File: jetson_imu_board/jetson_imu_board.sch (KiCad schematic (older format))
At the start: 9 parts

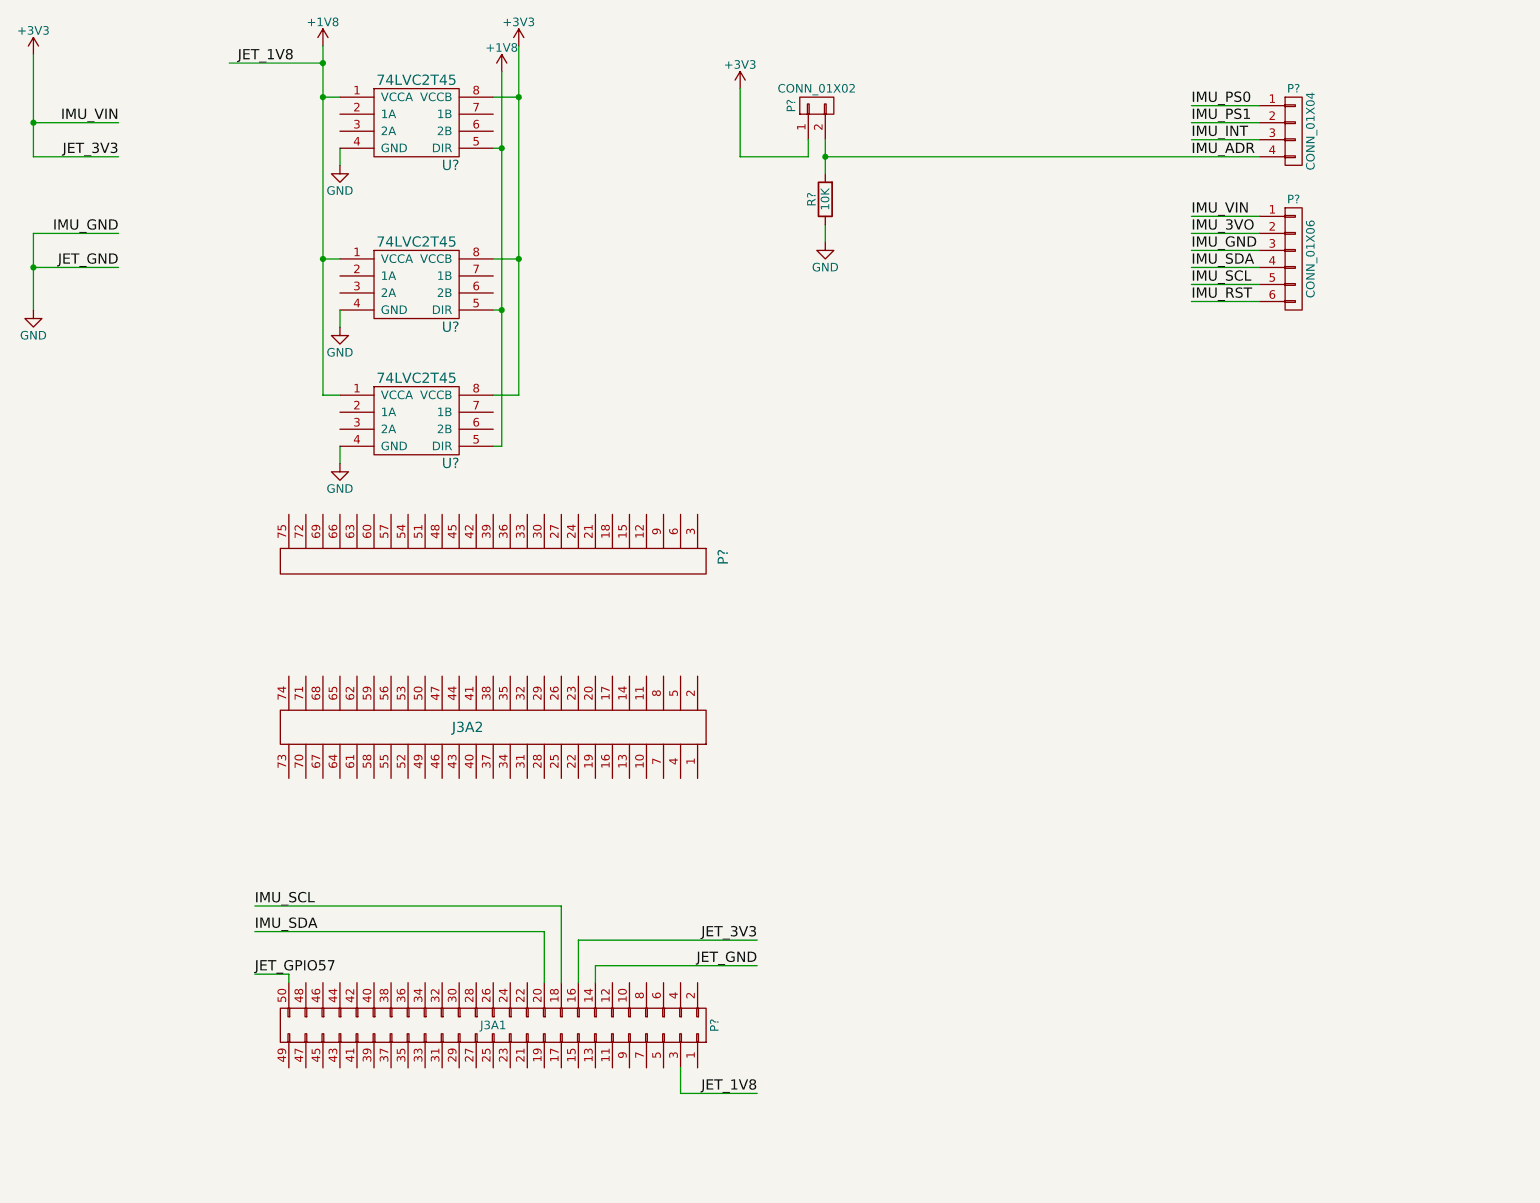
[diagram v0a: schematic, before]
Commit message: Switched to TXB0108 level shifter
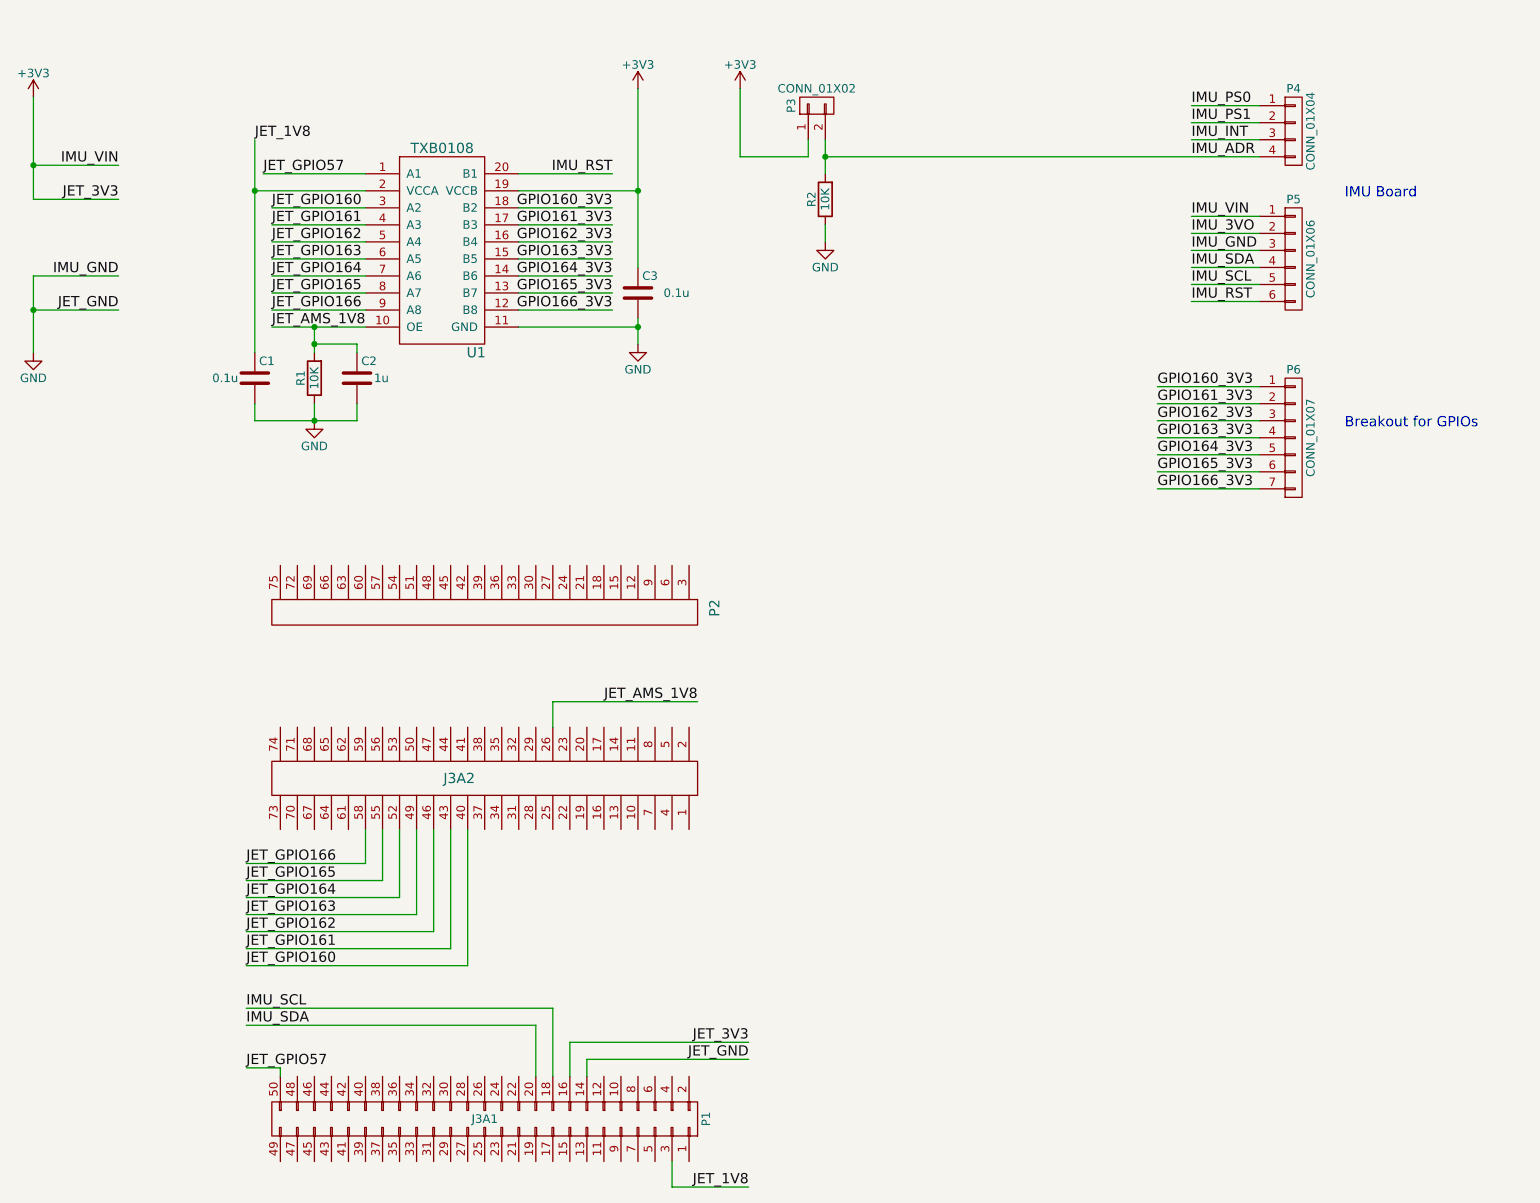
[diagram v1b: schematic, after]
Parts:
- removed U? (x3): 74LVC2T45, symbol 74LVC2T45
- added C1, C3: 0.1u, symbol C
- added C2: 1u, symbol C
- added P6: CONN_01X07, symbol CONN_01X07
- added R1: 10K, symbol R
- added U1: TXB0108, symbol TXB0108
- gave numbers to parts that had none: 6
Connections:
- net +3V3: now also C3.1, U1.19 (VCCB)
- net GND: now also C1.2, C2.2, C3.2, R1.1, U1.11 (GND)
- net IMU_RST: now also U1.20 (B1)
- net JET_GPIO57: now also U1.1 (A1)
- net JET_AMS_1V8: now reaches P2.26
- net JET_AMS_1V8: now also C2.1, R1.2, U1.10 (OE)
- net JET_GPIO160: now reaches P2.40
- net JET_GPIO160: now also U1.3 (A2)
- net JET_GPIO161: now reaches P2.43
- net JET_GPIO161: now also U1.4 (A3)
- net JET_GPIO162: now reaches P2.46
- net JET_GPIO162: now also U1.5 (A4)
- net JET_GPIO163: now reaches P2.49
- net JET_GPIO163: now also U1.6 (A5)
- net JET_GPIO164: now reaches P2.52
- net JET_GPIO164: now also U1.7 (A6)
- net JET_GPIO165: now reaches P2.55
- net JET_GPIO165: now also U1.8 (A7)
- net JET_GPIO166: now reaches P2.58
- net JET_GPIO166: now also U1.9 (A8)
- net +1V8 renamed JET_1V8
- net JET_1V8: now also C1.1, U1.2 (VCCA)
- new net GPIO160_3V3: P6.1 (P1), U1.18 (B2)
- new net GPIO161_3V3: P6.2 (P2), U1.17 (B3)
- new net GPIO162_3V3: P6.3 (P3), U1.16 (B4)
- new net GPIO163_3V3: P6.4 (P4), U1.15 (B5)
- new net GPIO164_3V3: P6.5 (P5), U1.14 (B6)
- new net GPIO165_3V3: P6.6 (P6), U1.13 (B7)
- new net GPIO166_3V3: P6.7 (P7), U1.12 (B8)
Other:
- note added: "Breakout for GPIOs"
- note added: "IMU Board"
- moved on the sheet: P1, P2

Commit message: Added footprint associations, started board layout
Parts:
- C1, C2, C3: footprint (none) -> Capacitors_SMD:C_1206_HandSoldering
- P1, P2: footprint (none) -> Pin_Headers:Pin_Header_Straight_2x25_Pitch2.00mm
- P3: footprint (none) -> Pin_Headers:Pin_Header_Straight_1x02
- P4: footprint (none) -> Pin_Headers:Pin_Header_Straight_1x04
- P5: footprint (none) -> Pin_Headers:Pin_Header_Straight_1x06
- P6: footprint (none) -> Pin_Headers:Pin_Header_Straight_1x07
- R1, R2: footprint (none) -> Resistors_SMD:R_1206_HandSoldering
- U1: footprint (none) -> Housings_SSOP:SSOP-20_4.4x6.5mm_Pitch0.65mm
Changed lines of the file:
@@
 F 0 "P1" H 3650 8350 50  0000 C CNN
 F 1 "J3A1" V 3650 7050 50  0000 C CNN
-F 2 "" H 3650 6300 50  0000 C CNN
+F 2 "Pin_Headers:Pin_Header_Straight_2x25_Pitch2.00mm" H 3650 6300 50  0001 C CNN
 F 3 "" H 3650 6300 50  0000 C CNN
 	1    3650 7050
@@
 F 0 "P2" H 4350 5600 60  0000 C CNN
 F 1 "J3A2" V 3350 4100 60  0000 C CNN
-F 2 "" H 4100 1950 60  0001 C CNN
+F 2 "Pin_Headers:Pin_Header_Straight_2x25_Pitch2.00mm" H 4100 1950 60  0001 C CNN
 F 3 "" H 4100 1950 60  0001 C CNN
 	1    3900 4500
@@
 F 0 "P4" H 8400 1500 50  0000 C CNN
 F 1 "CONN_01X04" V 8500 1250 50  0000 C CNN
-F 2 "" H 8400 1250 50  0000 C CNN
+F 2 "Pin_Headers:Pin_Header_Straight_1x04" H 8400 1250 50  0001 C CNN
 F 3 "" H 8400 1250 50  0000 C CNN
 	1    8400 1250
@@
 F 0 "P5" H 8400 2350 50  0000 C CNN
 F 1 "CONN_01X06" V 8500 2000 50  0000 C CNN
-F 2 "" H 8400 2000 50  0000 C CNN
+F 2 "Pin_Headers:Pin_Header_Straight_1x06" H 8400 2000 50  0001 C CNN
 F 3 "" H 8400 2000 50  0000 C CNN
 	1    8400 2000
@@
 IMU_RST
 $Comp
-L GND #PWR2
+L GND #PWR01
 U 1 1 580D6C71
 P 1000 2550
-F 0 "#PWR2" H 1000 2300 50  0001 C CNN
+F 0 "#PWR01" H 1000 2300 50  0001 C CNN
 F 1 "GND" H 1000 2400 50  0000 C CNN
 F 2 "" H 1000 2550 50  0000 C CNN
@@
 IMU_SDA
 $Comp
-L +3V3 #PWR1
+L +3V3 #PWR02
 U 1 1 580D6F0B
 P 1000 1050
-F 0 "#PWR1" H 1000 900 50  0001 C CNN
+F 0 "#PWR02" H 1000 900 50  0001 C CNN
 F 1 "+3V3" H 1000 1190 50  0000 C CNN
 F 2 "" H 1000 1050 50  0000 C CNN
@@
 F 0 "P3" H 5600 1250 50  0000 C CNN
 F 1 "CONN_01X02" V 5700 1100 50  0000 C CNN
-F 2 "" H 5600 1100 50  0000 C CNN
+F 2 "Pin_Headers:Pin_Header_Straight_1x02" H 5600 1100 50  0001 C CNN
 F 3 "" H 5600 1100 50  0000 C CNN
 	1    5600 1100
@@
 F 0 "R2" V 5730 1650 50  0000 C CNN
 F 1 "10K" V 5650 1650 50  0000 C CNN
-F 2 "" V 5580 1650 50  0000 C CNN
+F 2 "Resistors_SMD:R_1206_HandSoldering" V 5580 1650 50  0001 C CNN
 F 3 "" H 5650 1650 50  0000 C CNN
 	1    5650 1650
@@
 $EndComp
 $Comp
-L GND #PWR7
+L GND #PWR03
 U 1 1 580D740A
 P 5650 1900
-F 0 "#PWR7" H 5650 1650 50  0001 C CNN
+F 0 "#PWR03" H 5650 1650 50  0001 C CNN
 F 1 "GND" H 5650 1750 50  0000 C CNN
 F 2 "" H 5650 1900 50  0000 C CNN
@@
 $EndComp
 $Comp
-L +3V3 #PWR6
+L +3V3 #PWR04
 U 1 1 580D7475
 P 5150 1000
-F 0 "#PWR6" H 5150 850 50  0001 C CNN
+F 0 "#PWR04" H 5150 850 50  0001 C CNN
 F 1 "+3V3" H 5150 1140 50  0000 C CNN
 F 2 "" H 5150 1000 50  0000 C CNN
@@
 	8200 2250 7800 2250
 Wire Wire Line
-	1000 2100 1000 2300
-Wire Wire Line
-	1000 2300 1000 2550
+	1000 2100 1000 2550
 Wire Wire Line
 	1000 2100 1500 2100
@@
 	3950 6500 2250 6500
 Wire Wire Line
-	1000 1050 1000 1450
-Wire Wire Line
-	1000 1450 1000 1650
+	1000 1050 1000 1650
 Wire Wire Line
 	1000 1650 1500 1650
@@
 Connection ~ 1000 1450
 Wire Wire Line
-	5650 1300 5650 1400
-Wire Wire Line
-	5650 1400 5650 1500
+	5650 1300 5650 1500
 Wire Wire Line
 	5650 1400 8200 1400
@@
 F 0 "U1" H 3600 1450 60  0000 C CNN
 F 1 "TXB0108" H 3400 2650 60  0000 C CNN
-F 2 "" H 3400 1100 60  0001 C CNN
+F 2 "Housings_SSOP:SSOP-20_4.4x6.5mm_Pitch0.65mm" H 3400 1100 60  0001 C CNN
 F 3 "" H 3400 1100 60  0001 C CNN
 	1    3400 2000
@@
 	3850 1600 4550 1600
 Wire Wire Line
-	4550 1000 4550 1600
-Wire Wire Line
-	4550 1600 4550 2050
-$Comp
-L +3V3 #PWR4
+	4550 1000 4550 2050
+$Comp
+L +3V3 #PWR05
 U 1 1 580EBAD8
 P 4550 1000
-F 0 "#PWR4" H 4550 850 50  0001 C CNN
+F 0 "#PWR05" H 4550 850 50  0001 C CNN
 F 1 "+3V3" H 4550 1140 50  0000 C CNN
 F 2 "" H 4550 1000 50  0000 C CNN
@@
 F 0 "C3" H 4575 2300 50  0000 L CNN
 F 1 "0.1u" H 4700 2200 50  0000 L CNN
-F 2 "" H 4588 2050 50  0000 C CNN
+F 2 "Capacitors_SMD:C_1206_HandSoldering" H 4588 2050 50  0001 C CNN
 F 3 "" H 4550 2200 50  0000 C CNN
 	1    4550 2200
@@
 $EndComp
 $Comp
-L GND #PWR5
+L GND #PWR06
 U 1 1 580EBB51
 P 4550 2500
-F 0 "#PWR5" H 4550 2250 50  0001 C CNN
+F 0 "#PWR06" H 4550 2250 50  0001 C CNN
 F 1 "GND" H 4550 2350 50  0000 C CNN
 F 2 "" H 4550 2500 50  0000 C CNN
@@
 $EndComp
 Wire Wire Line
-	2300 1300 2300 1600
-Wire Wire Line
-	2300 1600 2300 2550
+	2300 1300 2300 2550
 Connection ~ 2300 1600
 Wire Wire Line
-	4550 2350 4550 2400
-Wire Wire Line
-	4550 2400 4550 2500
+	4550 2350 4550 2500
 Wire Wire Line
 	2350 1500 2950 1500
@@
 F 0 "C1" H 2325 2800 50  0000 L CNN
 F 1 "0.1u" H 2050 2700 50  0000 L CNN
-F 2 "" H 2338 2550 50  0000 C CNN
+F 2 "Capacitors_SMD:C_1206_HandSoldering" H 2338 2550 50  0001 C CNN
 F 3 "" H 2300 2700 50  0000 C CNN
 	1    2300 2700
@@
 F 0 "R1" V 2730 2700 50  0000 C CNN
 F 1 "10K" V 2650 2700 50  0000 C CNN
-F 2 "" V 2580 2700 50  0000 C CNN
+F 2 "Resistors_SMD:R_1206_HandSoldering" V 2580 2700 50  0001 C CNN
 F 3 "" H 2650 2700 50  0000 C CNN
 	1    2650 2700
@@
 $EndComp
 Wire Wire Line
-	2650 2400 2650 2500
-Wire Wire Line
-	2650 2500 2650 2550
-$Comp
-L GND #PWR3
+	2650 2400 2650 2550
+$Comp
+L GND #PWR07
 U 1 1 580EC104
 P 2650 2950
-F 0 "#PWR3" H 2650 2700 50  0001 C CNN
+F 0 "#PWR07" H 2650 2700 50  0001 C CNN
 F 1 "GND" H 2650 2800 50  0000 C CNN
 F 2 "" H 2650 2950 50  0000 C CNN
@@
 	2300 2850 2300 2950
 Wire Wire Line
-	2300 2950 2650 2950
-Wire Wire Line
-	2650 2950 2900 2950
+	2300 2950 2900 2950
 Wire Wire Line
 	2650 2850 2650 2950
 Wire Wire Line
-	2400 2400 2650 2400
-Wire Wire Line
-	2650 2400 2950 2400
+	2400 2400 2950 2400
 Connection ~ 2650 2400
 Wire Wire Line
@@
 F 0 "C2" H 2925 2800 50  0000 L CNN
 F 1 "1u" H 3000 2700 50  0000 L CNN
-F 2 "" H 2938 2550 50  0000 C CNN
+F 2 "Capacitors_SMD:C_1206_HandSoldering" H 2938 2550 50  0001 C CNN
 F 3 "" H 2900 2700 50  0000 C CNN
 	1    2900 2700
@@
 F 0 "P6" H 8400 3450 50  0000 C CNN
 F 1 "CONN_01X07" V 8500 3050 50  0000 C CNN
-F 2 "" H 8400 3050 50  0000 C CNN
+F 2 "Pin_Headers:Pin_Header_Straight_1x07" H 8400 3050 50  0001 C CNN
 F 3 "" H 8400 3050 50  0000 C CNN
 	1    8400 3050
